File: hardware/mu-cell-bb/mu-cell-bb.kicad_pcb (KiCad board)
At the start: 4 copper layers, 65 x 30 mm, 77 parts, among them IC1 SX1255IWLTRT, J1 TX, J2 RX, J3 EXT_CLK, J4 RPi GPIO, J5 IO, Q1 BC817-40W, Q2 BC817-40W, U1 24LC256, U2 LDK130M33R, Y1 32MHz

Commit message: late night PCB changes
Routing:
- net +5V: track 119.4 -> 118.5 mm
- net GND: vias 141 -> 143
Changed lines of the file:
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@@
 		(sheetname "/")
 		(sheetfile "mu-cell-bb.kicad_sch")
+		(zone_connect 2)
 		(attr through_hole exclude_from_bom)
 		(fp_circle
@@
 		(sheetname "/")
 		(sheetfile "mu-cell-bb.kicad_sch")
+		(zone_connect 2)
 		(attr through_hole exclude_from_bom)
 		(fp_circle
@@
 		(sheetname "/")
 		(sheetfile "mu-cell-bb.kicad_sch")
+		(zone_connect 2)
 		(attr through_hole exclude_from_bom)
 		(fp_circle
@@
 		(sheetname "/")
 		(sheetfile "mu-cell-bb.kicad_sch")
+		(zone_connect 2)
 		(attr through_hole exclude_from_bom)
 		(fp_circle
@@
 	)
 	(segment
-		(start 166.8659 108.966)
-		(end 142.9512 108.966)
-		(width 0.5)
-		(layer "B.Cu")
-		(net 2)
-	)
-	(segment
 		(start 128.9626 86.8172)
 		(end 131.5026 86.8172)
@@
 	)
 	(segment
+		(start 168.2883 110.3884)
+		(end 167.2723 109.3724)
+		(width 0.5)
+		(layer "B.Cu")
+		(net 2)
+	)
+	(segment
 		(start 143.9672 109.982)
 		(end 143.9672 112.5982)
@@
 	)
 	(segment
-		(start 127.6616 88.1182)
-		(end 128.9626 86.8172)
+		(start 144.5768 109.3724)
+		(end 143.9672 109.982)
 		(width 0.5)
 		(layer "B.Cu")
@@
 	)
 	(segment
-		(start 168.2883 110.3884)
-		(end 166.8659 108.966)
+		(start 167.2723 109.3724)
+		(end 144.5768 109.3724)
+		(width 0.5)
+		(layer "B.Cu")
+		(net 2)
+	)
+	(segment
+		(start 127.6616 88.1182)
+		(end 128.9626 86.8172)
 		(width 0.5)
 		(layer "B.Cu")
@@
 	)
 	(via
+		(at 142.9512 91.186)
+		(size 0.6)
+		(drill 0.35)
+		(layers "F.Cu" "B.Cu")
+		(net 3)
+	)
+	(via
 		(at 147.7772 102.989)
 		(size 0.6)
@@
 	)
 	(via
+		(at 137.0838 91.8464)
+		(size 0.6)
+		(drill 0.35)
+		(layers "F.Cu" "B.Cu")
+		(net 3)
+	)
+	(via
 		(at 133.223 98.3742)
 		(size 0.6)
@@
 	)
 	(segment
-		(start 138.2844 92.7354)
-		(end 141.6626 89.3572)
+		(start 135.509 91.0336)
+		(end 139.9862 91.0336)
 		(width 0.25)
 		(layer "F.Cu")
@@
 	)
 	(segment
-		(start 133.8072 92.7354)
-		(end 138.2844 92.7354)
+		(start 131.6736 98.262399)
+		(end 131.6736 94.869)
 		(width 0.25)
 		(layer "F.Cu")
@@
 	)
 	(segment
-		(start 131.6736 94.869)
-		(end 133.8072 92.7354)
+		(start 139.9862 91.0336)
+		(end 141.6626 89.3572)
 		(width 0.25)
 		(layer "F.Cu")
@@
 	)
 	(segment
-		(start 131.6736 98.262399)
-		(end 131.6736 94.869)
+		(start 131.6736 94.869)
+		(end 135.509 91.0336)
 		(width 0.25)
 		(layer "F.Cu")
@@
 		(polygon
 			(pts
-				(xy 185.5978 91.62825) (xy 185.6232 84.5312) (xy 120.4976 84.582) (xy 120.4976 114.6302) (xy 185.6232 114.6302)
+				(xy 185.5978 91.62825) (xy 185.6232 84.5312) (xy 120.4976 84.5312) (xy 120.4976 114.6302) (xy 185.6232 114.6302)
 				(xy 185.5978 107.5432) (xy 181.3978 107.5432) (xy 174.9658 108.472) (xy 157.6658 108.472) (xy 157.6658 91.172)
 				(xy 174.9658 91.172) (xy 181.3978 91.62825)

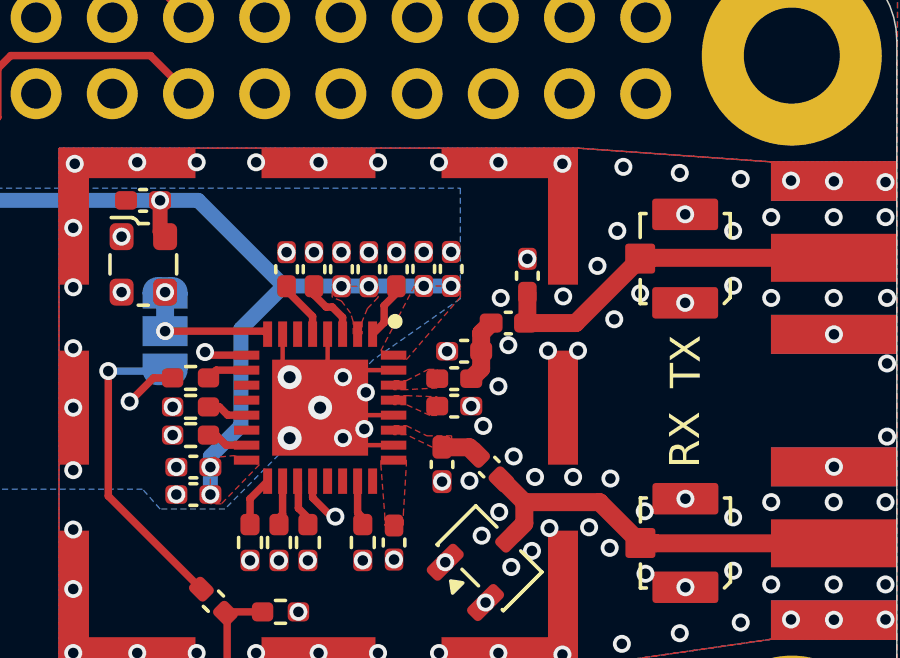
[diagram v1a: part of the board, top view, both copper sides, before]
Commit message: updated silkscreens on PCB
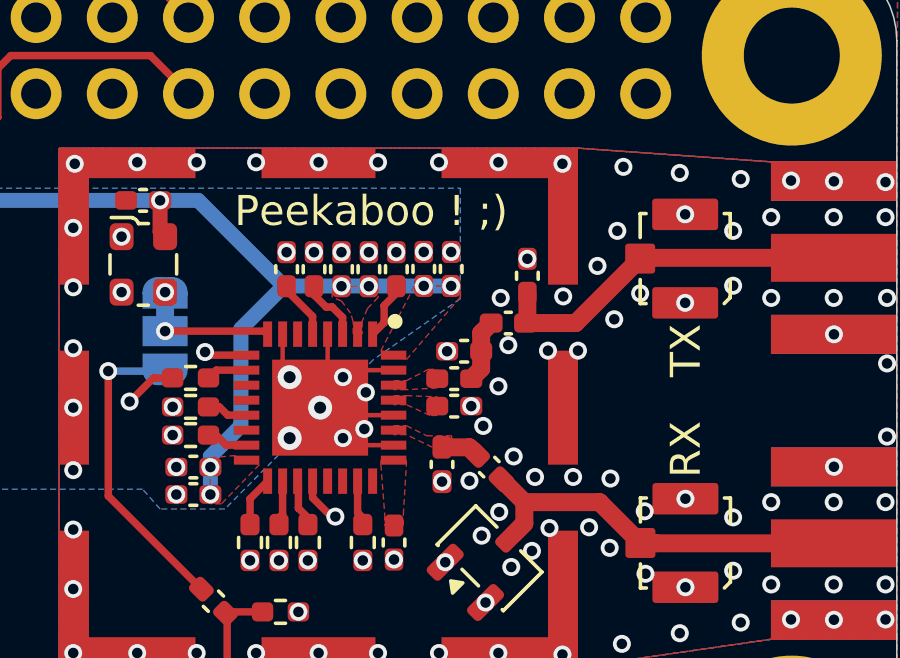
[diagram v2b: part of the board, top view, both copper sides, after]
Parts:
- removed BE000000: ~, OSHW:OSHW-Certification-Mark-Stacked_8x7mm_SilkMask
- added BE000024: ~, OSHW:OSHW-Certification-Mark-Stacked_8x7mm_SilkMask, B.Cu at (135.6, 99.6)
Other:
- board text added: "Peekaboo ! ;)"

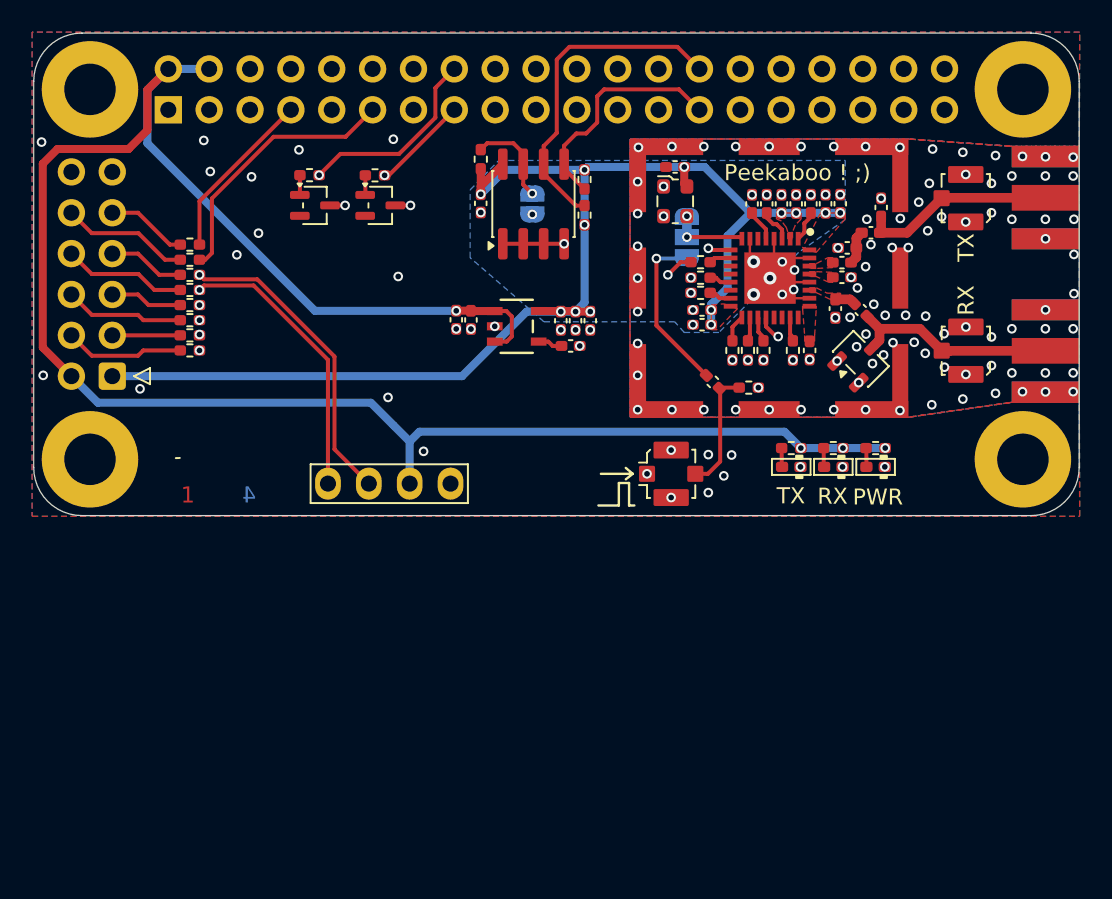
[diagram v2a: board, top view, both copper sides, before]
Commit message: updated TX and RX front ends
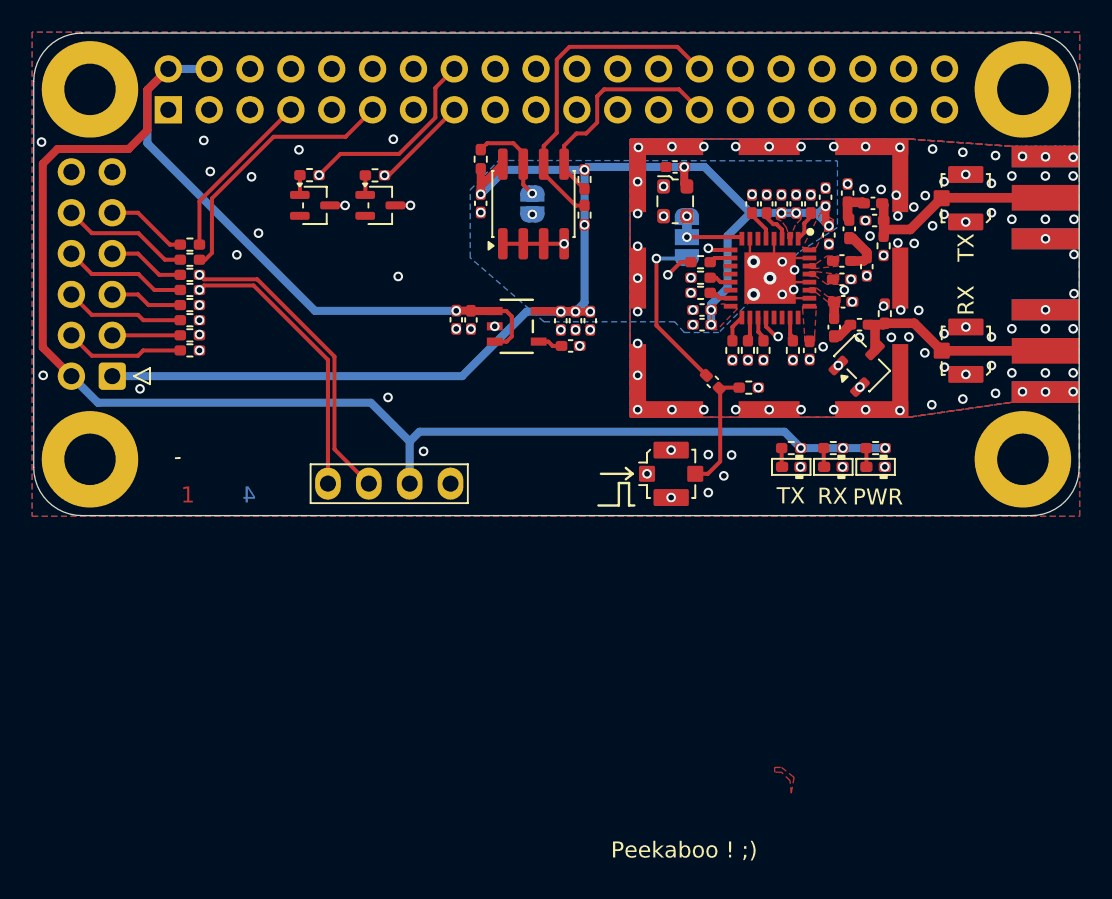
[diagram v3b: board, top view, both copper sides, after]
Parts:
- added C4: 8.2p, Capacitor_SMD:C_0402_1005Metric_Pad0.74x0.62mm_HandSolder, F.Cu at (171.2, 94.5)
- added C6: 100p, Capacitor_SMD:C_0402_1005Metric_Pad0.74x0.62mm_HandSolder, F.Cu at (171.9, 102.7)
- added L4: 39n, Inductor_SMD:L_0402_1005Metric_Pad0.77x0.64mm_HandSolder, F.Cu at (170.9, 101.3)
- added R8: 1M, Resistor_SMD:R_0402_1005Metric_Pad0.72x0.64mm_HandSolder, F.Cu at (173.4, 97.8)
- added R9: 1M, Resistor_SMD:R_0402_1005Metric_Pad0.72x0.64mm_HandSolder, F.Cu at (173.5, 102.0)
- C1: value 33p -> 100p
- C2: value 6.8p -> 100p
- C3: value 6.8p -> 3.3p
- C5: value 27p -> 6.8p
- L1: value 33n -> 39n
- L2: value 39n -> 22n
- L3: value 82n -> 39n
- moved L2 6.67 mm to (172.8, 95.2), turned to 0 degrees
- moved C5 4.07 mm to (172.9, 96.2), turned to 180 degrees
- moved C3 3.79 mm to (172.4, 99.1), turned to -90 degrees
- moved C2 1.98 mm to (170.8, 99.9), turned to 0 degrees
- moved C17 1.96 mm to (170.0, 97.1), turned to -90 degrees
- moved L1 1.37 mm to (171.3, 96.8), turned to 90 degrees
- moved L3 1.16 mm to (170.4, 102.9)
- moved C16 1.00 mm to (169.8, 94.8)
- moved D1 0.29 mm to (172.1, 105.1)
- moved C1 0.10 mm to (170.8, 98.8)
- renumbered C8 to C10, C9 to C11, C10 to C12, C11 to C13, C12 to C14, C13 to C15, C14 to C16, C15 to C17, C16 to C18, C17 to C19, C18 to C20, C19 to C21, C20 to C22, C21 to C23, C22 to C24, C23 to C25, C6 to C7, C4 to C8, C7 to C9, R8 to R10, R9 to R11, R10 to R12, R11 to R13, R12 to R14, R14 to R16, R13 to R17, R16 to R18, R17 to R19, R18 to R20, R19 to R21, R20 to R22, R21 to R23, R22 to R24, R23 to R25, R24 to R26
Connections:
- C2 pad 1: Net-(C1-Pad2) -> /RFO_N
- C3 pad 1: /RF_TX -> Net-(C1-Pad2)
- C5 pad 1: /RFO_N -> /RF_TX
- L1 pad 2: /RF_TX -> Net-(C4-Pad1)
- L2 pad 1: /RF_RX -> Net-(C4-Pad1)
- L2 pad 2: /RFI -> /RF_TX
- L3 pad 1: GND -> Net-(C6-Pad1)
- R15 pad 2: Net-(LED3-A) -> Net-(LED2-A)
- R17 pad 2: Net-(LED2-A) -> Net-(LED3-A)
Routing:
- net Net-(C4-Pad1): track 0.00 -> 2.16 mm
- net +3V3: track 80.2 -> 81.8 mm
- net Net-(C6-Pad1): track 0.00 -> 1.31 mm
- net /RF_TX: track 12.2 -> 13.0 mm
- net Net-(C1-Pad2): track 2.13 -> 2.85 mm

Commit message: updated PCB
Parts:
- moved JP1 1.84 mm to (162.5, 96.0), turned to 0 degrees
- moved C2 0.08 mm to (170.8, 99.8)
- moved C1 0.05 mm to (170.8, 98.8)
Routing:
- net +3V3: track 81.8 -> 92.6 mm
- net GND: track 17.8 -> 24.1 mm, vias 143 -> 145
- net /EXT_CLK: track 10.5 -> 14.9 mm
- net /SX_CLK: track 3.46 -> 2.70 mm
- net /CK_OUT: track 31.8 -> 31.2 mm
- net /RST: track 10.9 -> 11.4 mm

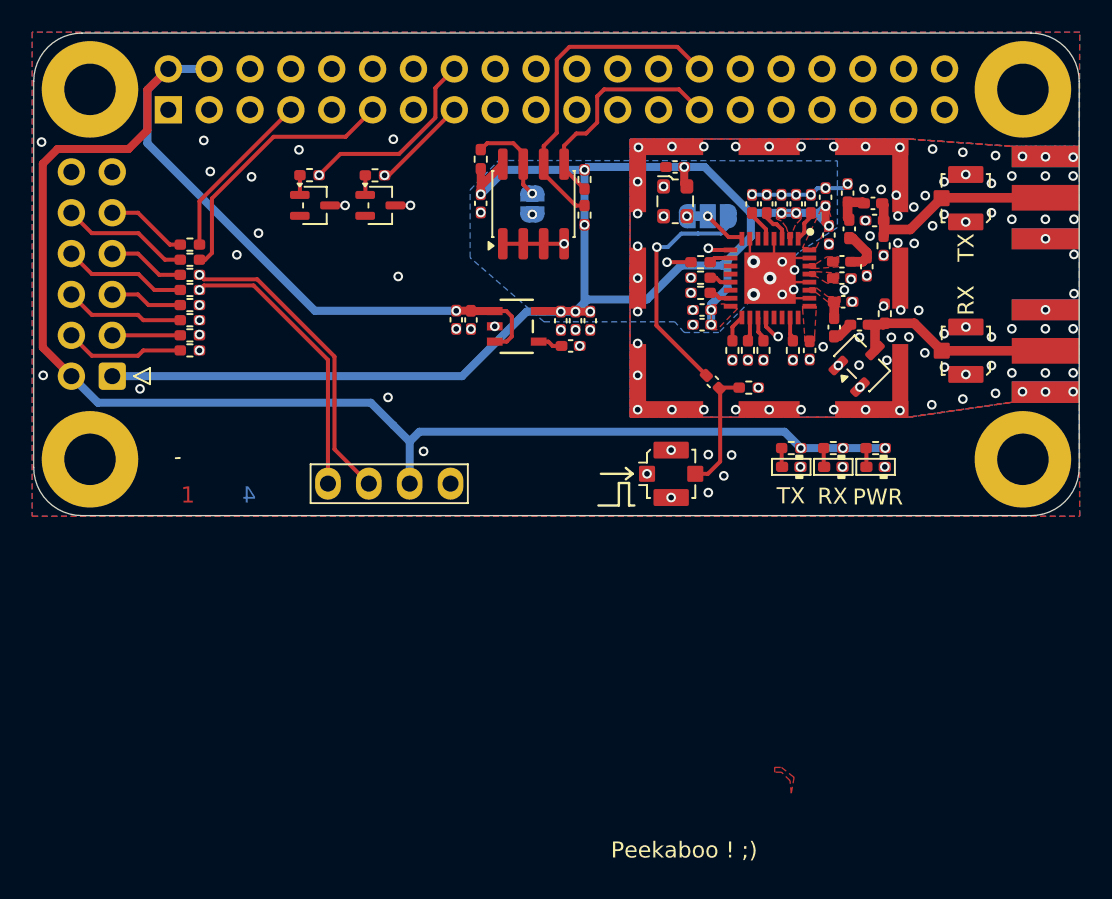
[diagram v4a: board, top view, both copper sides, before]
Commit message: added eeprom programming header, updated part numbers
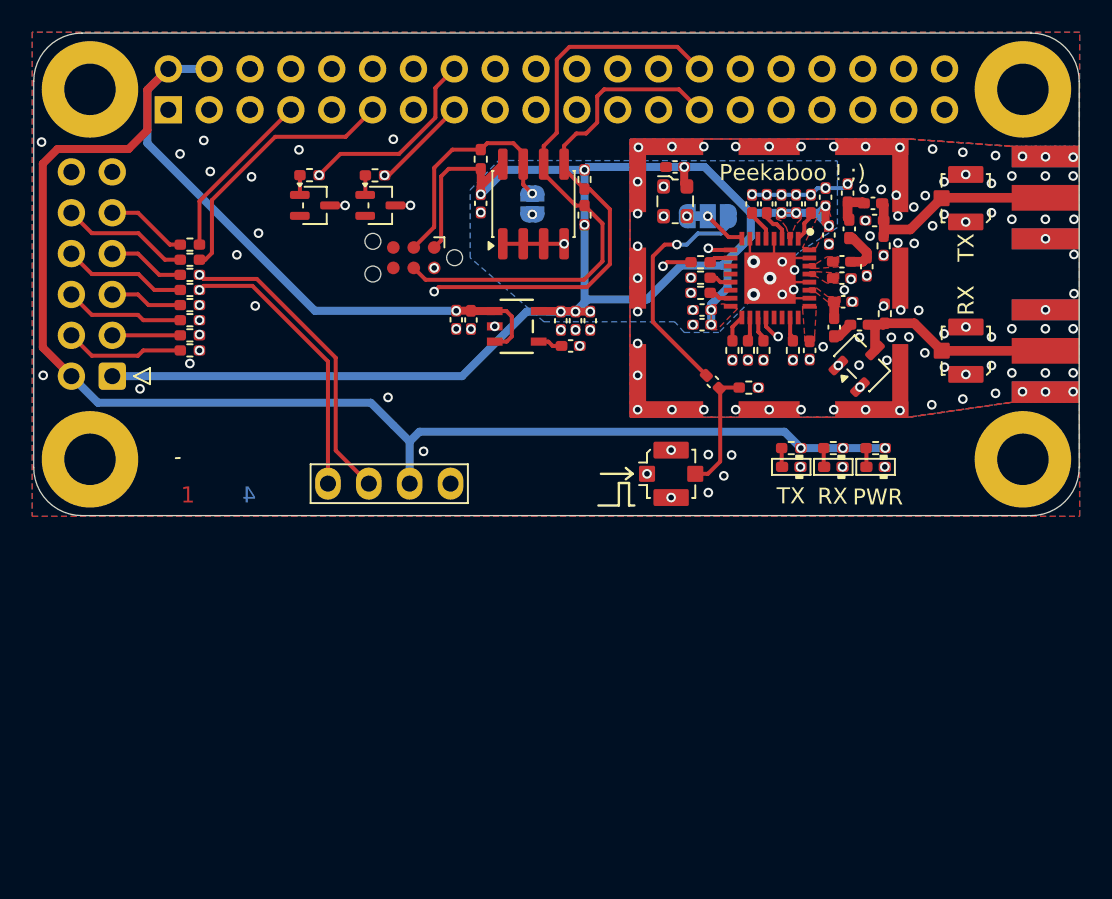
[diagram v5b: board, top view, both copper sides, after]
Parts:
- added J6: TC2030, Connector:Tag-Connect_TC2030-IDC-NL_2x03_P1.27mm_Vertical, F.Cu at (144.2, 98.6)
- LED1: value Green -> Red
- LED2: value Red -> Amber
- LED3: value Yellow -> Green
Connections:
- net Net-(JP2-A) renamed /WP
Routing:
- net /ID_SD: track 14.6 -> 33.2 mm, vias 0 -> 2
- net /ID_SC: track 20.6 -> 37.0 mm
- net /WP: track 5.81 -> 14.6 mm
- net +3V3: track 92.6 -> 99.9 mm
- net /RST: track 11.4 -> 16.8 mm
- net /~{CS}: track 28.9 -> 32.9 mm
- net /CK_OUT: track 31.2 -> 32.3 mm
- net GND: vias 145 -> 147

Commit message: made final changes before ordering first batch
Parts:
- added J7: TC2030, Connector:Tag-Connect_TC2030-IDC-NL_2x03_P1.27mm_Vertical, B.Cu at (144.2, 98.6)
- LED2: renamed from LED3; value Green -> Amber
- LED3: renamed from LED2; value Amber -> Green
- Y1: value 32MHz -> 38.4MHz
- moved L4 4.97 mm to (171.2, 106.3), turned to 90 degrees
- moved L3 3.81 mm to (172.8, 105.8), turned to 180 degrees
- moved D1 2.48 mm to (171.2, 102.8), turned to 90 degrees
- moved C6 2.12 mm to (173.4, 104.2), turned to 90 degrees
- moved R9 0.08 mm to (173.4, 102.0)
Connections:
- D1 pad 3: /RF_RX -> /RFI
- LED2 pad 1: Net-(LED3-K) -> Net-(LED2-K)
- LED2 pad 2: Net-(LED3-A) -> Net-(LED2-A)
- LED3 pad 1: Net-(LED2-K) -> Net-(LED3-K)
- LED3 pad 2: Net-(LED2-A) -> Net-(LED3-A)
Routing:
- net +3V3: track 99.9 -> 109.6 mm
- net /WP: track 14.6 -> 22.6 mm, vias 1 -> 3
- net /ID_SC: track 37.0 -> 44.2 mm, vias 0 -> 1
- net Net-(LED3-K): track 44.1 -> 39.5 mm
- net /ID_SD: track 33.2 -> 37.3 mm
- net /RFI: track 1.01 -> 5.07 mm
- net /~{CS}: track 32.9 -> 35.7 mm
- net Net-(LED2-K): track 36.2 -> 38.4 mm
- net /RF_RX: track 13.3 -> 11.8 mm
- net GND: vias 147 -> 153

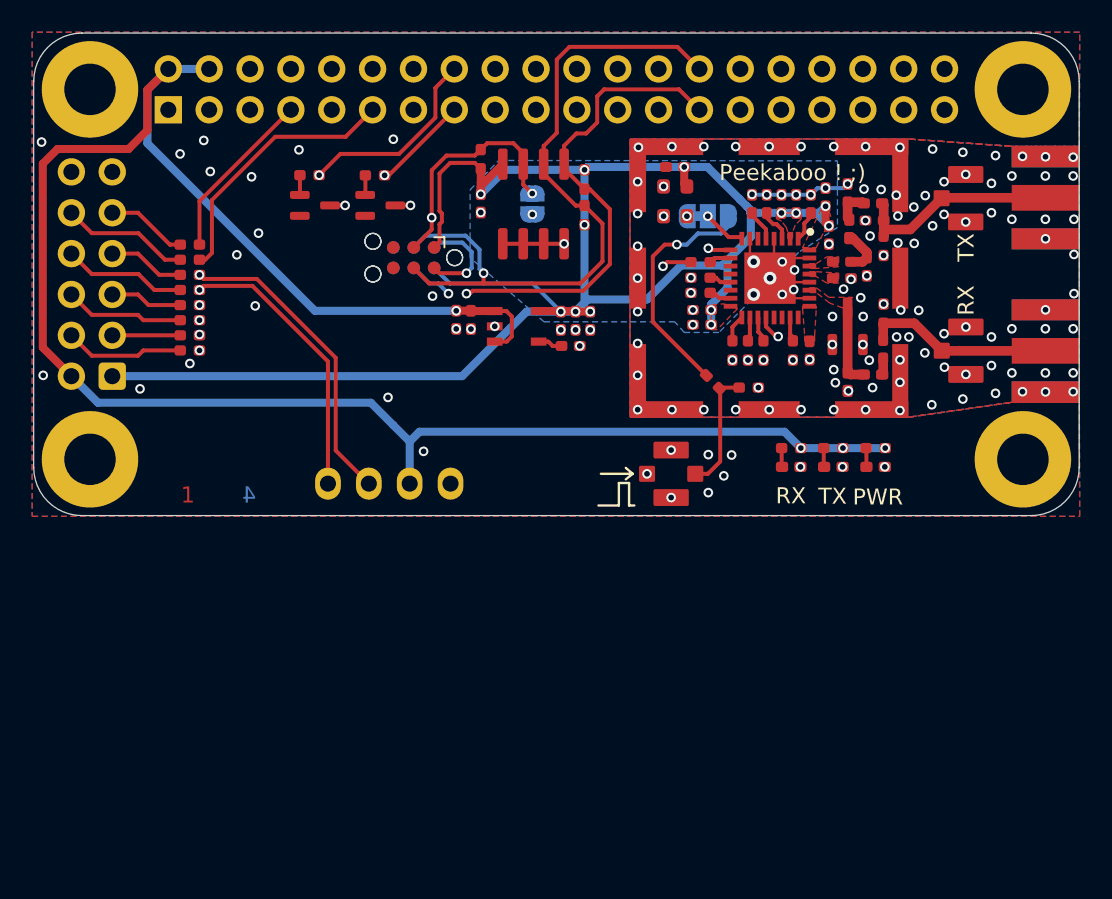
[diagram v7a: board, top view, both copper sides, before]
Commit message: added muCell-BB v1.1 files
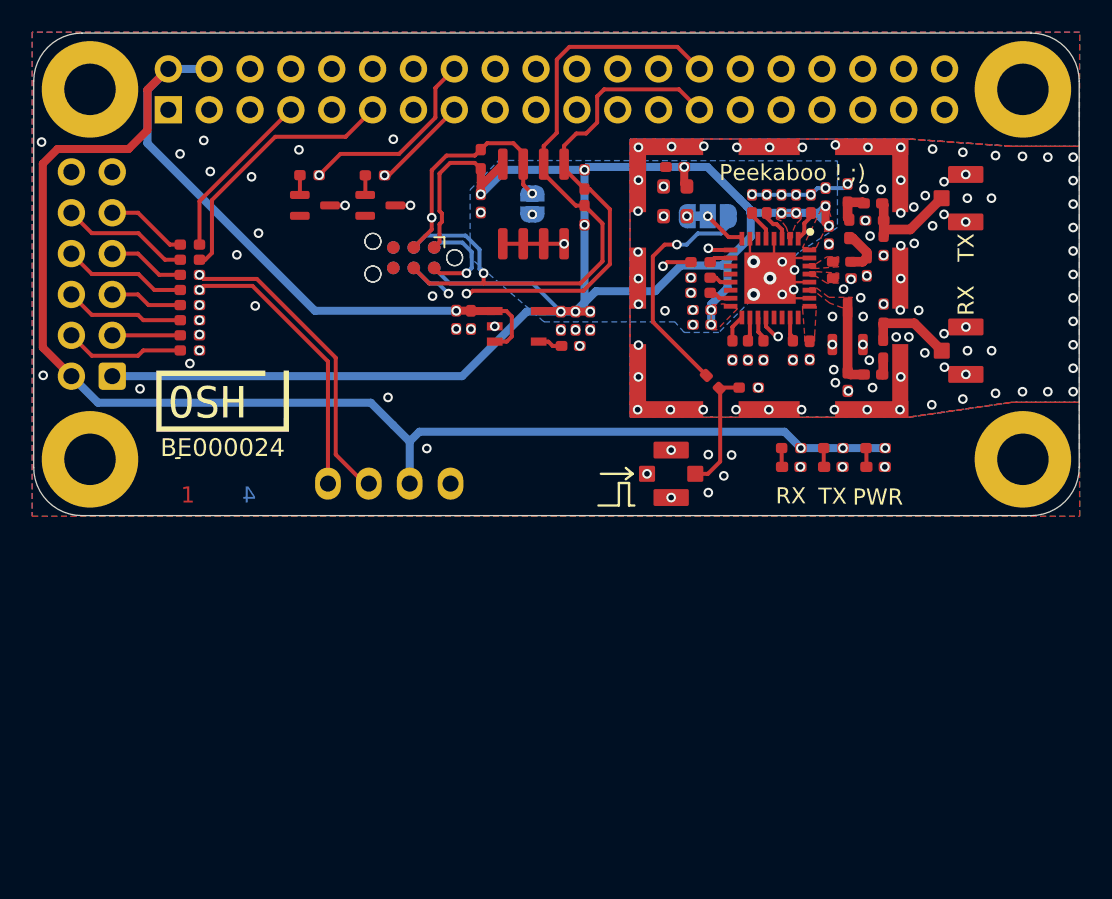
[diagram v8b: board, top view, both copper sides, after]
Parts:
- removed JSMA1: TX, parts:BATWIRELESS_BWSMA-KE-P001
- removed JSMA2: RX, parts:BATWIRELESS_BWSMA-KE-P001
- added BE000024: ~, OSHW:OSHW-Certification-Mark-Stacked_8x7mm_SilkMask, F.Cu at (132.3, 108.0)
- moved BE000024 21.1 mm to (154.9, 108.0), turned to 180 degrees
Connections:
- J6 pad 6: unconnected-(J6-Pad6) -> GND
- J7 pad 6: unconnected-(J7-Pad6) -> GND
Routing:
- net /RF_TX: track 13.0 -> 6.49 mm
- net /RF_RX: track 11.8 -> 5.38 mm
- net /~{CS}: track 35.7 -> 34.7 mm
- net /CK_OUT: track 32.3 -> 31.3 mm
- net GND: vias 153 -> 147
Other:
- board text added: "Serial n°"
